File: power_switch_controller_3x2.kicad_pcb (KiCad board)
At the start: 2 copper layers, 69.8 x 40.6 mm, 1 part

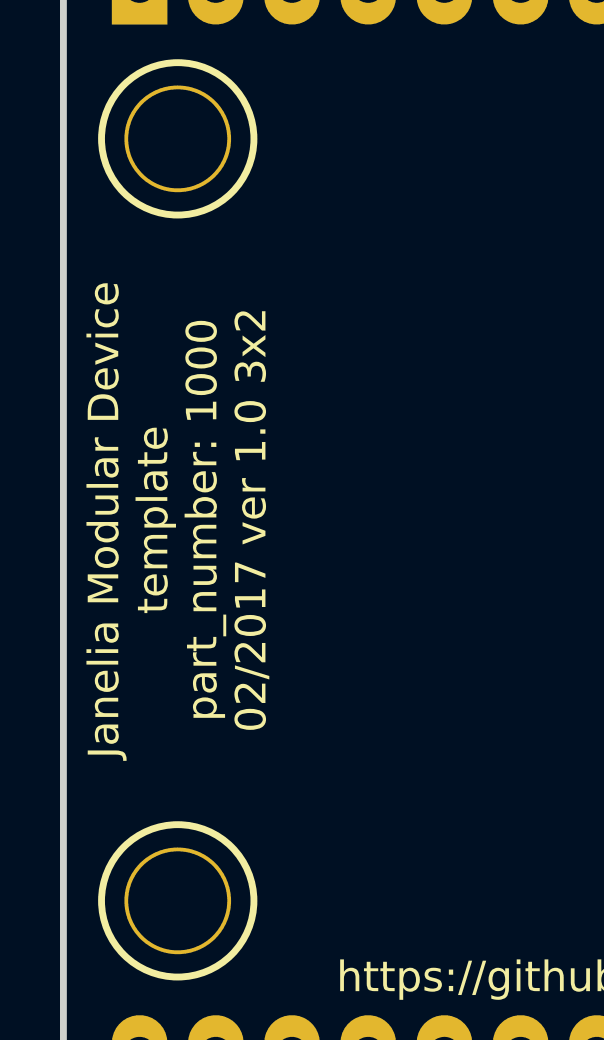
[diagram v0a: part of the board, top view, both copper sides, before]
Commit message: template -> power_switch_controller.
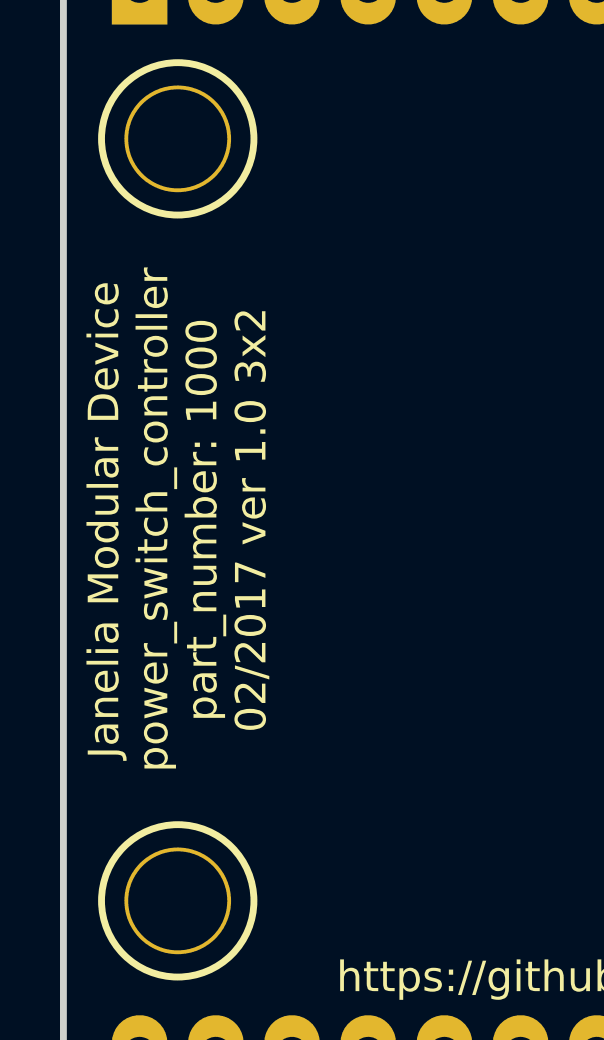
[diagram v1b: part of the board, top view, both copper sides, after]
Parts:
- MDB1: footprint template_3x2:MODULAR_DEVICE_BASE_3X2_MALE -> power_switch_controller_3x2:MODULAR_DEVICE_BASE_3X2_MALE
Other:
- board text added: "Janelia Modular Device power_switch_controller part_number: 1000 02/2017 ver 1.0 3x2"
- board text removed: "Janelia Modular Device template part_number: 1000 02/2017 ver 1.0 3x2"
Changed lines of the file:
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@@
   (page A4)
   (title_block
-    (title template_3x2)
+    (title power_switch_controller_3x2)
     (rev 1.0)
   )
@@
     (diff_pair_width 0.254)
   )
-  (module template_3x2:MODULAR_DEVICE_BASE_3X2_MALE (layer F.Cu)
+  (module power_switch_controller_3x2:MODULAR_DEVICE_BASE_3X2_MALE (layer F.Cu)
     (at 107.315 88.9)
     (fp_text reference MDB1 (at 0 0) (layer F.SilkS) hide
@@
     (effects (font (size 1.016 1.016) (thickness 0.1905)))
   )
-  (gr_text "Janelia Modular Device\ntemplate\npart_number: 1000\n02/2017 ver 1.0 3x2" (at 89.535 88.9 90) (layer F.SilkS)
+  (gr_text "Janelia Modular Device\npower_switch_controller\npart_number: 1000\n02/2017 ver 1.0 3x2" (at 89.535 88.9 90) (layer F.SilkS)
     (effects (font (size 1.016 1.016) (thickness 0.254)))
   )

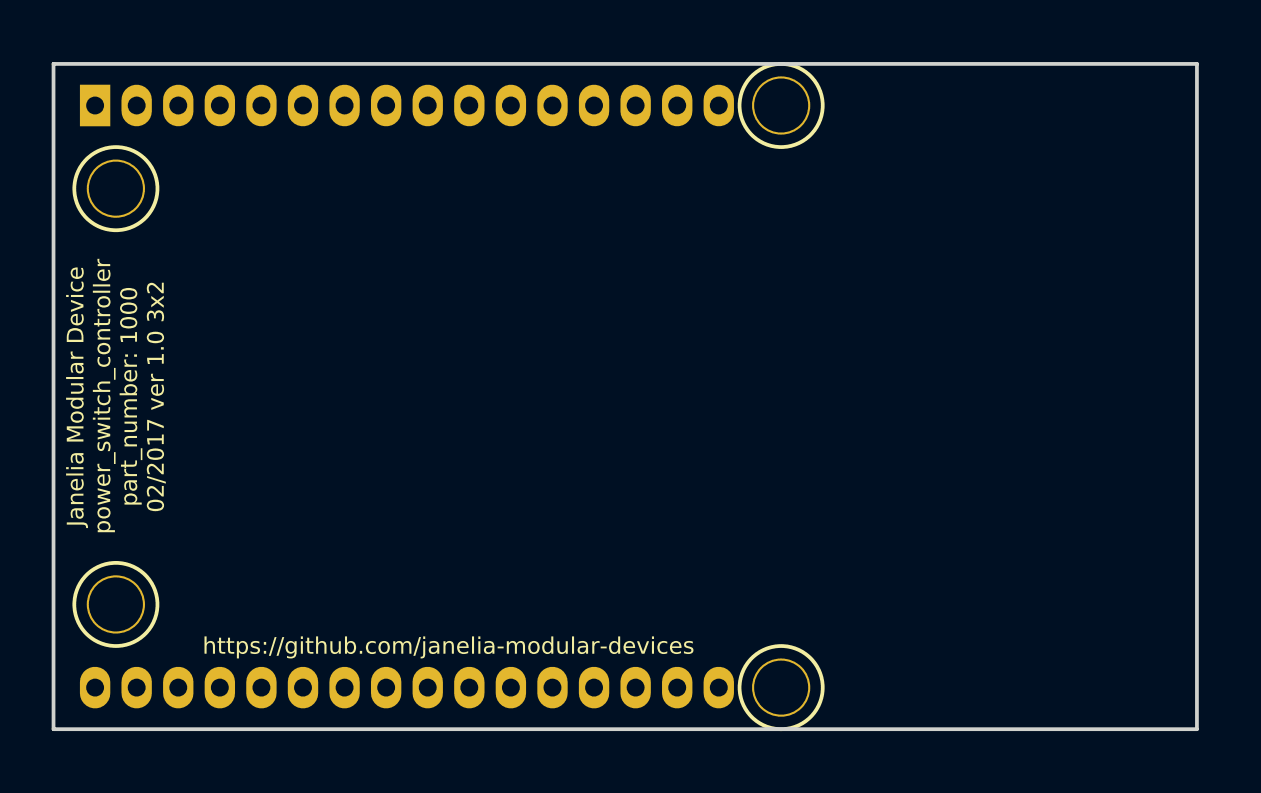
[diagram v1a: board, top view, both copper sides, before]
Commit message: Added footprints and components.
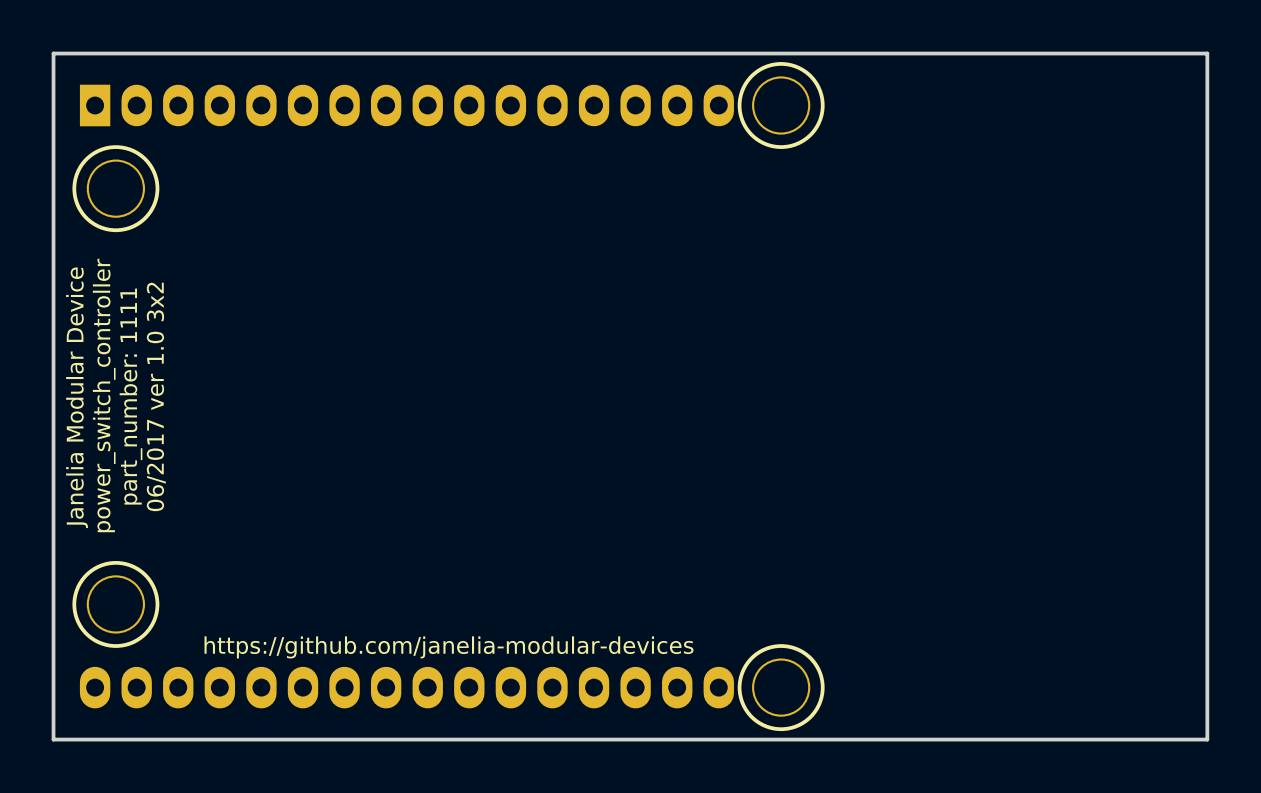
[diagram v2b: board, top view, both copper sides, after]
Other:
- board size 69.8 x 40.6 mm -> 70.5 x 41.9 mm
- board text added: "Janelia Modular Device power_switch_controller part_number: 1111 06/2017 ver 1.0 3x2"
- board text removed: "Janelia Modular Device power_switch_controller part_number: 1000 02/2017 ver 1.0 3x2"

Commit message: Finished v1.0.
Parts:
- added C1: 10uF, power_switch_controller_3x2:SM1210, B.Cu at (95.9, 85.7)
- added C2: 0.1uF, power_switch_controller_3x2:SM1210, B.Cu at (130.2, 100.3)
- added D1: diode_schottky_45V_10A, power_switch_controller_3x2:CFP15, B.Cu at (145.4, 79.4)
- added L1: LED_24V, power_switch_controller_3x2:LED_555-3XXX, F.Cu at (149.2, 104.8)
- added L2: LED_24V, power_switch_controller_3x2:LED_555-3XXX, F.Cu at (118.7, 96.5)
- added L3: LED_24V, power_switch_controller_3x2:LED_555-3XXX, F.Cu at (116.2, 96.5)
- added L4: LED_24V, power_switch_controller_3x2:LED_555-3XXX, F.Cu at (113.7, 96.5)
- added L5: LED_24V, power_switch_controller_3x2:LED_555-3XXX, F.Cu at (111.1, 96.5)
- added L6: LED_24V, power_switch_controller_3x2:LED_555-3XXX, F.Cu at (108.6, 96.5)
- added L7: LED_24V, power_switch_controller_3x2:LED_555-3XXX, F.Cu at (106.0, 96.5)
- added L8: LED_24V, power_switch_controller_3x2:LED_555-3XXX, F.Cu at (103.5, 96.5)
- added L9: LED_24V, power_switch_controller_3x2:LED_555-3XXX, F.Cu at (101.0, 96.5)
- added P1: PWR_JACK_2.5x5.5, power_switch_controller_3x2:DCJACK_2PIN_HIGHCURRENT, F.Cu at (156.2, 88.9)
- added P2: HEADER_02X08_SMD, power_switch_controller_3x2:HEADER_02x08_SMD, F.Cu at (109.9, 85.7)
- added SW1: SPST_SLIDE_AS, power_switch_controller_3x2:SPST_SLIDE_AS, F.Cu at (149.2, 101.0)
- added U1: TLE7230R, power_switch_controller_3x2:PG-DSO-36, B.Cu at (130.2, 88.9)
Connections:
- MDB1 pad 10: (no net) -> /CS
- MDB1 pad 11: (no net) -> /MOSI
- MDB1 pad 12: (no net) -> /MISO
- MDB1 pad 13: (no net) -> /SCK
- MDB1 pad 2: (no net) -> /RESET
- MDB1 pad 6: (no net) -> /PWM_0
- MDB1 pad GND: (no net) -> GND
- MDB1 pad VDD: (no net) -> VDD
- MDB1 pad VEE: (no net) -> VEE
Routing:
- net GND: track 0.00 -> 173.7 mm, vias 0 -> 1
- net VDD: track 0.00 -> 146.7 mm, vias 0 -> 3
- net VEE: track 0.00 -> 88.6 mm
- net /RESET: track 0.00 -> 52.7 mm, vias 0 -> 1
- net /PWM_0: track 0.00 -> 51.5 mm
- net LED_PWR: track 0.00 -> 50.9 mm
- net /CS: track 0.00 -> 36.1 mm
- net /channels_0-7/OUT_3: track 0.00 -> 34.8 mm, vias 0 -> 1
- net /channels_0-7/OUT_2: track 0.00 -> 32.0 mm, vias 0 -> 1
- net /channels_0-7/OUT_7: track 0.00 -> 31.6 mm
- net /channels_0-7/OUT_1: track 0.00 -> 30.8 mm
- net /channels_0-7/OUT_6: track 0.00 -> 28.7 mm
- net /channels_0-7/OUT_0: track 0.00 -> 27.8 mm
- net /channels_0-7/OUT_5: track 0.00 -> 23.7 mm
- net /channels_0-7/OUT_4: track 0.00 -> 21.0 mm
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- added copper zone on B.Cu, net GND
- added copper zone on F.Cu, net VDD
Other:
- board text added: "+"
- board text added: "-"
- board text added: "0"
- board text added: "1"
- board text added: "2"
- board text added: "2.5x5.5 Center + +9-42VDC"
- board text added: "3"
- board text added: "4"
- board text added: "5"
- board text added: "6"
- board text added: "7"
- board text added: "Lights"

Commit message: Version 1.1.
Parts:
- added D2: diode_low_rev_current, power_switch_controller_3x2:SOD-123, B.Cu at (118.7, 99.7)
- added D3: diode_low_rev_current, power_switch_controller_3x2:SOD-123, B.Cu at (116.2, 99.7)
- added D4: diode_low_rev_current, power_switch_controller_3x2:SOD-123, B.Cu at (113.7, 99.7)
- added D5: diode_low_rev_current, power_switch_controller_3x2:SOD-123, B.Cu at (111.1, 99.7)
- added D6: diode_low_rev_current, power_switch_controller_3x2:SOD-123, B.Cu at (108.6, 99.7)
- added D7: diode_low_rev_current, power_switch_controller_3x2:SOD-123, B.Cu at (106.0, 99.7)
- added D8: diode_low_rev_current, power_switch_controller_3x2:SOD-123, B.Cu at (103.5, 99.7)
- added D9: diode_low_rev_current, power_switch_controller_3x2:SOD-123, B.Cu at (101.0, 99.7)
- moved L2 3.17 mm to (118.7, 93.3)
- moved L3 3.17 mm to (116.2, 93.3)
- moved L4 3.17 mm to (113.7, 93.3)
- moved L5 3.17 mm to (111.1, 93.3)
- moved L6 3.17 mm to (108.6, 93.3)
- moved L7 3.17 mm to (106.0, 93.3)
- moved L8 3.17 mm to (103.5, 93.3)
- moved L9 3.17 mm to (101.0, 93.3)
- moved C1 1.91 mm to (95.9, 83.8)
- moved P2 1.91 mm to (109.9, 83.8)
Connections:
- net /PWM_0 renamed /MAP
- L2 pad 1: LED_PWR -> /channels_0-7/LP_0
- L3 pad 1: LED_PWR -> /channels_0-7/LP_1
- L4 pad 1: LED_PWR -> /channels_0-7/LP_2
- L5 pad 1: LED_PWR -> /channels_0-7/LP_3
- L6 pad 1: LED_PWR -> /channels_0-7/LP_4
- L7 pad 1: LED_PWR -> /channels_0-7/LP_5
- L8 pad 1: LED_PWR -> /channels_0-7/LP_6
- L9 pad 1: LED_PWR -> /channels_0-7/LP_7
- MDB1 pad 5: (no net) -> /IN
- U1 pad 12: VEE -> /IN
- U1 pad 6: VEE -> /IN
- U1 pad 7: VEE -> /IN
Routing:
- net /IN: track 0.00 -> 63.1 mm
- net VDD: track 146.7 -> 124.6 mm, vias 3 -> 0
- net VEE: track 88.6 -> 74.6 mm, vias 0 -> 2
- net GND: track 173.7 -> 178.4 mm
- net /channels_0-7/OUT_7: track 31.6 -> 29.0 mm
- net /channels_0-7/OUT_6: track 28.7 -> 26.2 mm
- net /CS: track 36.1 -> 34.0 mm, vias 0 -> 1
- net /channels_0-7/LP_7: track 0.00 -> 2.11 mm
- net /channels_0-7/LP_6: track 0.00 -> 2.11 mm
- net /channels_0-7/LP_5: track 0.00 -> 2.11 mm
- net /channels_0-7/LP_4: track 0.00 -> 2.11 mm
- net /channels_0-7/LP_3: track 0.00 -> 2.11 mm
- net /channels_0-7/LP_2: track 0.00 -> 2.11 mm
- net /channels_0-7/LP_1: track 0.00 -> 2.11 mm
- net /channels_0-7/LP_0: track 0.00 -> 2.11 mm
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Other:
- board text added: "2.5x5.5 Center + +12-42VDC"
- board text added: "Janelia Modular Device power_switch_controller part_number: 1111 07/2017 ver 1.1 3x2"
- board text removed: "2.5x5.5 Center + +9-42VDC"
- board text removed: "Janelia Modular Device power_switch_controller part_number: 1111 06/2017 ver 1.0 3x2"
